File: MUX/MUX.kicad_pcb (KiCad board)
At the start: 4 copper layers, 364 x 203 mm, 135 parts, among them P1 Conn_02x36_Top_Bottom, P2 DB9_Male, P3 DB9_Male, P4 DB9_Male, P5 DB9_Male

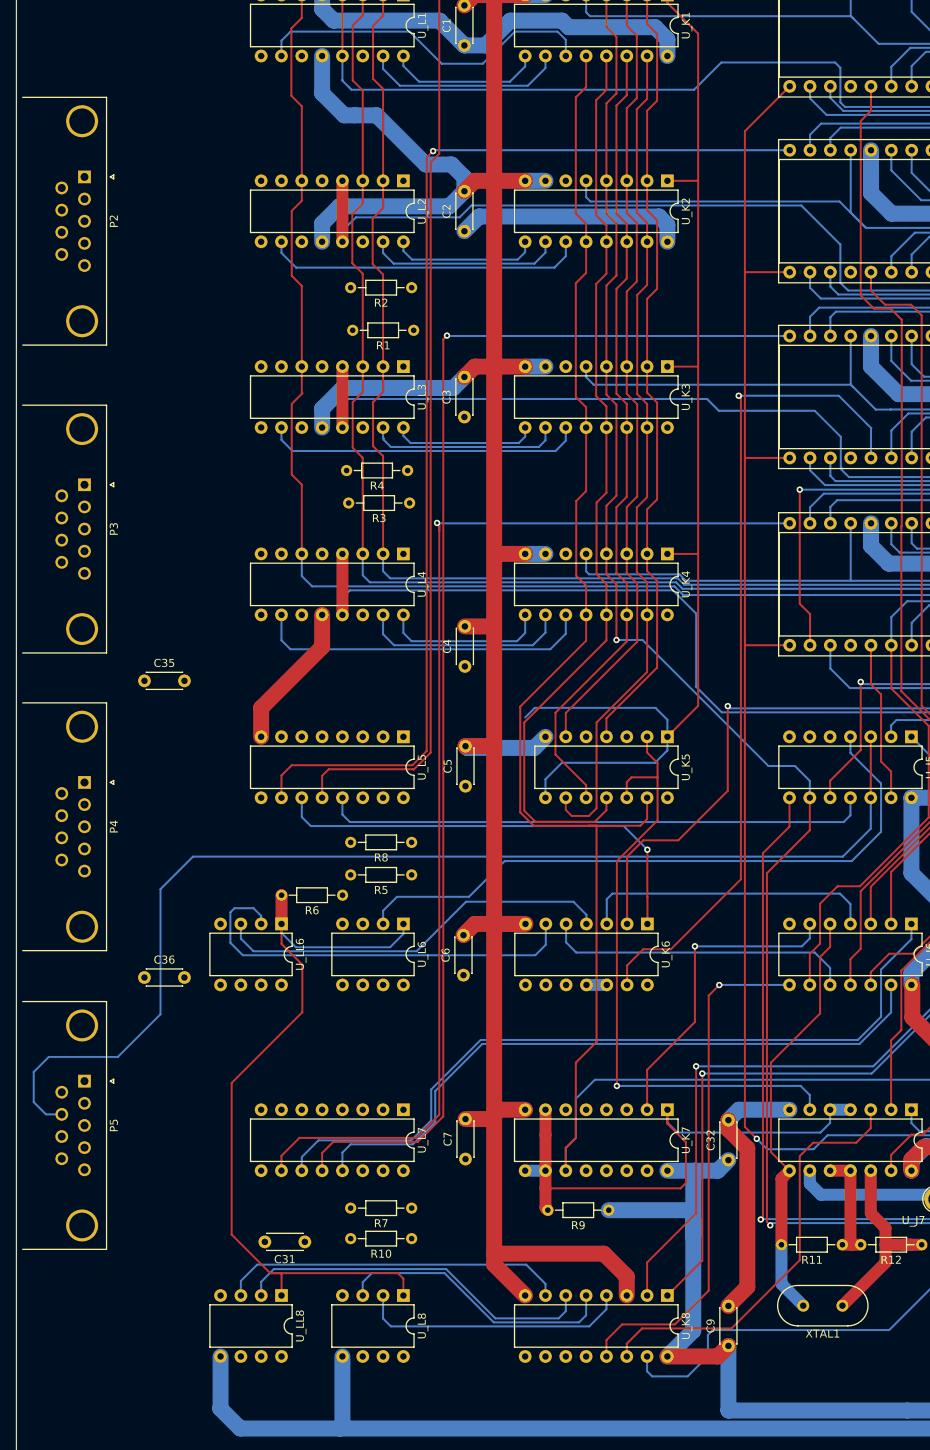
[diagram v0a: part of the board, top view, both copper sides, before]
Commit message: MUX: Add connector pinout switch jumpers
Provide jumper blocks to easily confiure MUX outputs as either Centuriobn native
or standard RS232 pinout. Provides for ease of use of USB adapters,
off-the-shelf cables, etc.
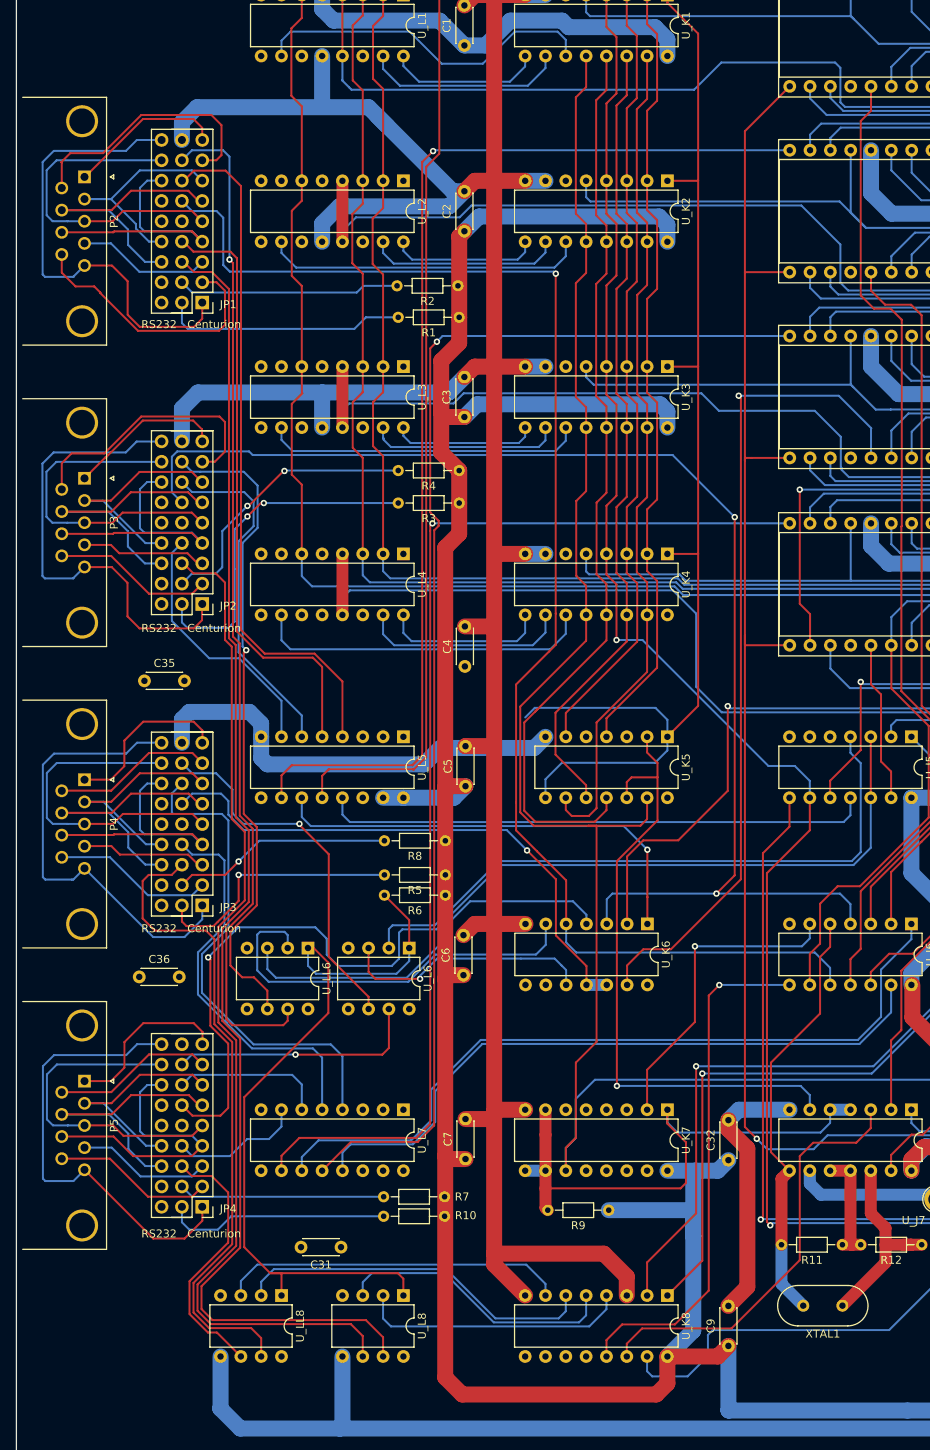
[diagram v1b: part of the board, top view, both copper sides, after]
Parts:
- added JP1: Jumper_3x9_Bridged12, Connector_PinHeader_2.54mm:PinHeader_3x09_P2.54mm_Vertical, F.Cu at (47.2, 79.1)
- added JP2: Jumper_3x9_Bridged12, Connector_PinHeader_2.54mm:PinHeader_3x09_P2.54mm_Vertical, F.Cu at (47.2, 116.8)
- added JP3: Jumper_3x9_Bridged12, Connector_PinHeader_2.54mm:PinHeader_3x09_P2.54mm_Vertical, F.Cu at (47.2, 154.4)
- added JP4: Jumper_3x9_Bridged12, Connector_PinHeader_2.54mm:PinHeader_3x09_P2.54mm_Vertical, F.Cu at (47.2, 192.1)
- moved R6 12.9 mm to (77.6, 153.2)
- moved R4 6.45 mm to (79.3, 100.1)
- moved R3 6.20 mm to (79.3, 104.1)
- moved R1 5.92 mm to (79.3, 80.9)
- moved R2 5.80 mm to (79.2, 77.0)
- moved R10 4.97 mm to (77.5, 193.3)
- moved C31 4.57 mm to (64.6, 197.2)
- moved U_LL6 4.48 mm to (60.5, 159.8)
- moved R7 4.35 mm to (77.5, 190.9)
- moved R8 4.22 mm to (77.6, 146.4)
- moved R5 4.22 mm to (77.6, 150.6)
- moved U_L6 3.10 mm to (73.1, 159.8)
- moved P3 0.80 mm to (32.5, 101.0)
- moved C36 0.65 mm to (39.4, 163.4)
- moved P4 0.34 mm to (32.5, 138.7)
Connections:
- P2 pad 1: GND -> Net-(JP1-Pad25)
- P2 pad 2: /~{CTS_{0}} -> Net-(JP1-Pad12)
- P2 pad 3: -12V -> Net-(JP1-Pad13)
- P2 pad 4: /~{RTS_{0}} -> Net-(JP1-Pad7)
- P2 pad 5: Net-(P2-Pad5) -> Net-(JP1-Pad1)
- P2 pad 6: /~{TX_{0}} -> Net-(JP1-Pad22)
- P2 pad 7: /~{TX_{0}_EIA} -> Net-(JP1-Pad16)
- P2 pad 8: /~{RX_{0}} -> Net-(JP1-Pad10)
- P2 pad 9: Net-(P2-Pad9) -> Net-(JP1-Pad4)
- P3 pad 1: GND -> Net-(P3-Pad1)
- P3 pad 2: /~{CTS_{1}} -> Net-(JP2-Pad12)
- P3 pad 3: -12V -> Net-(P3-Pad3)
- P3 pad 4: /~{RTS_{1}} -> Net-(P3-Pad4)
- P3 pad 6: /~{TX_{1}} -> Net-(P3-Pad6)
- P3 pad 7: /~{TX_{1}_EIA} -> Net-(JP2-Pad16)
- P3 pad 8: /~{RX_{1}} -> Net-(P3-Pad8)
- P4 pad 1: GND -> Net-(P4-Pad1)
- P4 pad 2: /~{CTS_{2}} -> Net-(JP3-Pad12)
- P4 pad 3: -12V -> Net-(P4-Pad3)
- P4 pad 4: /~{RTS_{2}} -> Net-(P4-Pad4)
- P4 pad 6: /~{TX_{2}} -> Net-(P4-Pad6)
- P4 pad 7: /~{TX_{2}_EIA} -> Net-(P4-Pad7)
- P4 pad 8: /~{RX_{2}} -> Net-(P4-Pad8)
- P5 pad 1: GND -> Net-(P5-Pad1)
- P5 pad 2: /~{CTS_{3}} -> Net-(P5-Pad2)
- P5 pad 3: -12V -> Net-(P5-Pad3)
- P5 pad 4: /~{RTS_{3}} -> Net-(P5-Pad4)
- P5 pad 6: /~{TX_{3}} -> Net-(P5-Pad6)
- P5 pad 7: /~{TX_{3}_EIA} -> Net-(P5-Pad7)
- P5 pad 8: /~{RX_{3}} -> Net-(P5-Pad8)
- R1 pad 2: Net-(P2-Pad5) -> Net-(JP1-Pad2)
- R10 pad 2: Net-(P5-Pad5) -> Net-(R10-Pad2)
- R2 pad 2: Net-(P2-Pad9) -> Net-(JP1-Pad5)
- R3 pad 2: Net-(P3-Pad5) -> Net-(R3-Pad2)
- R4 pad 2: Net-(P3-Pad9) -> Net-(JP2-Pad5)
- R5 pad 2: Net-(P4-Pad5) -> Net-(R5-Pad2)
- R7 pad 2: Net-(P5-Pad9) -> Net-(R7-Pad2)
- R8 pad 2: Net-(P4-Pad9) -> Net-(R8-Pad2)
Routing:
- net +5V: track 3327.7 -> 3557.8 mm
- net /~{RTS_{0}}: track 0.00 -> 167.4 mm
- net /~{TX_{0}_EIA}: track 38.8 -> 178.7 mm, vias 0 -> 1
- net /~{TX_{1}_EIA}: track 36.9 -> 165.1 mm, vias 0 -> 2
- net /~{RTS_{1}}: track 0.00 -> 127.2 mm
- net /~{TX_{0}}: track 0.00 -> 126.9 mm, vias 0 -> 1
- net /~{CTS_{0}}: track 0.00 -> 86.4 mm
- net /~{RTS_{2}}: track 0.00 -> 82.2 mm
- net /~{TX_{1}}: track 0.00 -> 82.0 mm, vias 0 -> 1
- net /~{RX_{0}}: track 0.00 -> 75.6 mm
- net GND: track 2840.1 -> 2914.3 mm
- net /~{TX_{2}_EIA}: track 2.54 -> 70.0 mm, vias 0 -> 1
- net /~{CTS_{2}}: track 0.00 -> 62.1 mm
- net Net-(P3-Pad5): track 0.00 -> 58.8 mm
- net Net-(JP1-Pad1): track 0.00 -> 58.8 mm
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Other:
- board text added: "RS232 Centurion"

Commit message: MUX: More power routing
All basic connections except 12V
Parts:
- moved C34 3.05 mm to (173.1, 119.7)
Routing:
- net GND: track 2914.3 -> 3322.5 mm, vias 4 -> 5
- net +5V: track 3557.8 -> 3790.0 mm
- net +12V: track 315.0 -> 355.2 mm
- net Net-(U_K1-Pad1): track 149.2 -> 128.2 mm
- net -12V: track 398.5 -> 415.7 mm
- net /LoadCR_{3}: track 200.1 -> 207.3 mm
- net /~{TX_{3}_EIA}: track 136.0 -> 143.1 mm
- net /Data.InBD_{2}: track 535.7 -> 542.8 mm
- net /~{RX_{3}}: track 16.6 -> 22.5 mm
- net /Data.OutD_{5}: track 417.0 -> 422.7 mm, vias 3 -> 4
- net Net-(U_E6-Pad1): track 29.9 -> 25.3 mm
- net Net-(U_J6-Pad8): track 64.9 -> 69.3 mm
- net Net-(U_H7-Pad15): track 227.8 -> 232.1 mm
- net /~{TX_{1}_EIA}: track 165.1 -> 169.4 mm
- net /Data.InBD_{6}: track 464.2 -> 467.8 mm
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
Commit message: MUX: Connections completed
All traces done
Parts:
- moved C8 15.4 mm to (112.5, 36.3)
- moved C35 4.39 mm to (44.4, 126.6)
- moved C36 3.61 mm to (43.0, 163.6)
- moved JP4 2.02 mm to (45.2, 192.1)
- moved JP1 2.02 mm to (45.2, 79.1)
- moved JP2 2.02 mm to (45.2, 116.8)
- moved JP3 2.02 mm to (45.2, 154.4)
- moved C31 0.18 mm to (64.8, 197.2)
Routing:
- net -12V: track 415.7 -> 756.0 mm, vias 2 -> 6
- net GND: track 3322.5 -> 3573.8 mm, vias 5 -> 7
- net +12V: track 355.2 -> 562.0 mm, vias 1 -> 2
- net +5V: track 3790.0 -> 3909.1 mm
- net /~{RX_{2}}: track 50.0 -> 59.4 mm
- net /~{CTS_{2}}: track 62.1 -> 71.5 mm
- net Net-(P5-Pad1): track 21.6 -> 14.6 mm
- net Net-(U_A1-Pad10): track 79.6 -> 73.0 mm
- net Net-(R6-Pad2): track 95.8 -> 102.3 mm
- net Sys.INT_OUT: track 117.4 -> 111.0 mm
- net Net-(P1-Pad30): track 0.00 -> 5.90 mm, vias 0 -> 1
- net Net-(JP1-Pad12): track 28.9 -> 24.4 mm
- net Net-(P5-Pad3): track 41.3 -> 37.2 mm
- net Net-(P4-Pad3): track 41.3 -> 37.2 mm
- net Net-(JP1-Pad13): track 41.3 -> 37.3 mm
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
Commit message: MUX: Proper crystal
Use HC-49U crystal. Elements rearranged to match the original layout, just for
fun. Some more power optimizations.
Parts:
- XTAL1: footprint Crystal:Crystal_HC18-U_Vertical -> Crystal:Crystal_HC49-U_Horizontal
- moved R20 19.6 mm to (146.8, 199.5)
- moved R21 8.71 mm to (141.7, 180.6), turned to -90 degrees
- moved XTAL1 6.25 mm to (124.5, 198.9), turned to 0 degrees
- moved TP1 4.99 mm to (142.5, 194.7)
- moved R11 2.18 mm to (127.3, 194.7)
- moved R12 2.18 mm to (137.2, 194.7)
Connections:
- JP4 pad 15: (no net) -> unconnected-(JP4-Pad15)
- JP4 pad 18: (no net) -> unconnected-(JP4-Pad18)
- JP4 pad 3: (no net) -> unconnected-(JP4-Pad3)
- JP4 pad 6: (no net) -> unconnected-(JP4-Pad6)
- XTAL1 pad 1: Net-(R12-Pad1) -> Net-(R11-Pad2)
- XTAL1 pad 2: Net-(R11-Pad2) -> Net-(R12-Pad1)
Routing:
- net GND: track 3573.8 -> 3761.5 mm
- net +5V: track 3909.1 -> 3839.5 mm
- net /MUXClock: track 441.5 -> 451.2 mm
- net Net-(R21-Pad2): track 20.7 -> 28.5 mm
- net Net-(R12-Pad1): track 24.4 -> 19.1 mm
- net Net-(U_J7-Pad6): track 78.8 -> 84.0 mm
- net Net-(R20-Pad2): track 10.9 -> 16.0 mm
- net Net-(U_H7-Pad15): track 230.7 -> 227.1 mm
- net Net-(U_H7-Pad9): track 120.0 -> 117.0 mm
- net Net-(R11-Pad2): track 51.4 -> 48.6 mm
- net Net-(R11-Pad1): track 14.1 -> 11.9 mm
- net /RxD_{2}: track 106.1 -> 104.4 mm
- net /RX_{3}_IN: track 141.9 -> 143.3 mm
- net /RX_{1}_IN: track 142.0 -> 143.3 mm
- net /Data.InBD_{1}: track 544.2 -> 545.5 mm
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
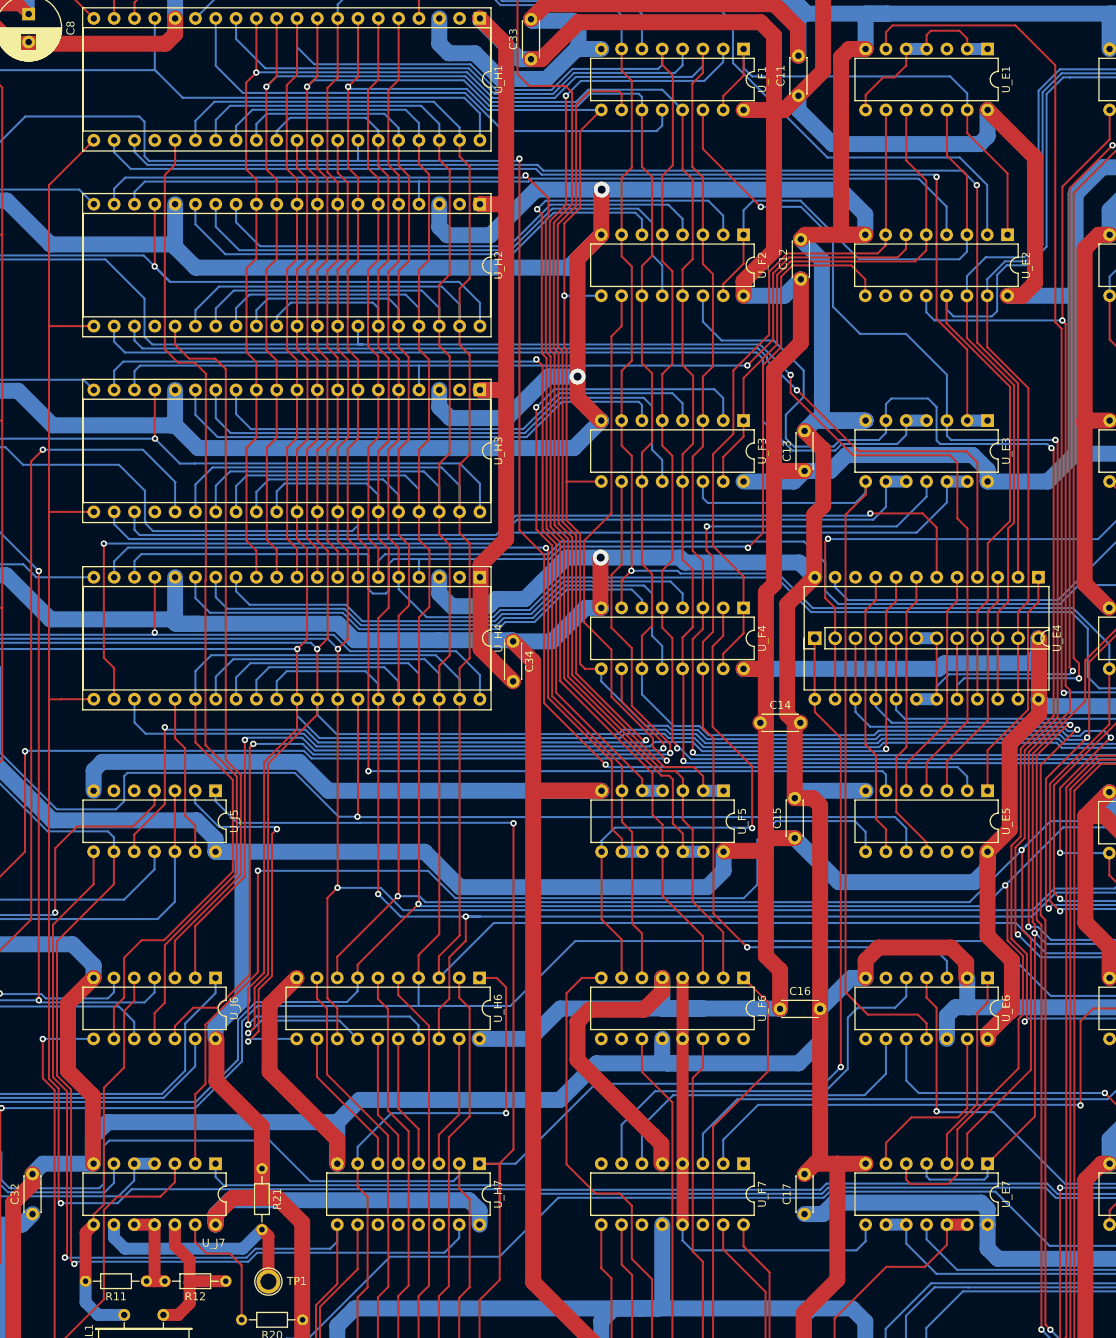
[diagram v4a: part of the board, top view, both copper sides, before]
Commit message: MUX: Fix DRC errors
Rearranged U_E4 socket and extra row in order to avoid overlap errors. Fixed up
jumper block courtyards.
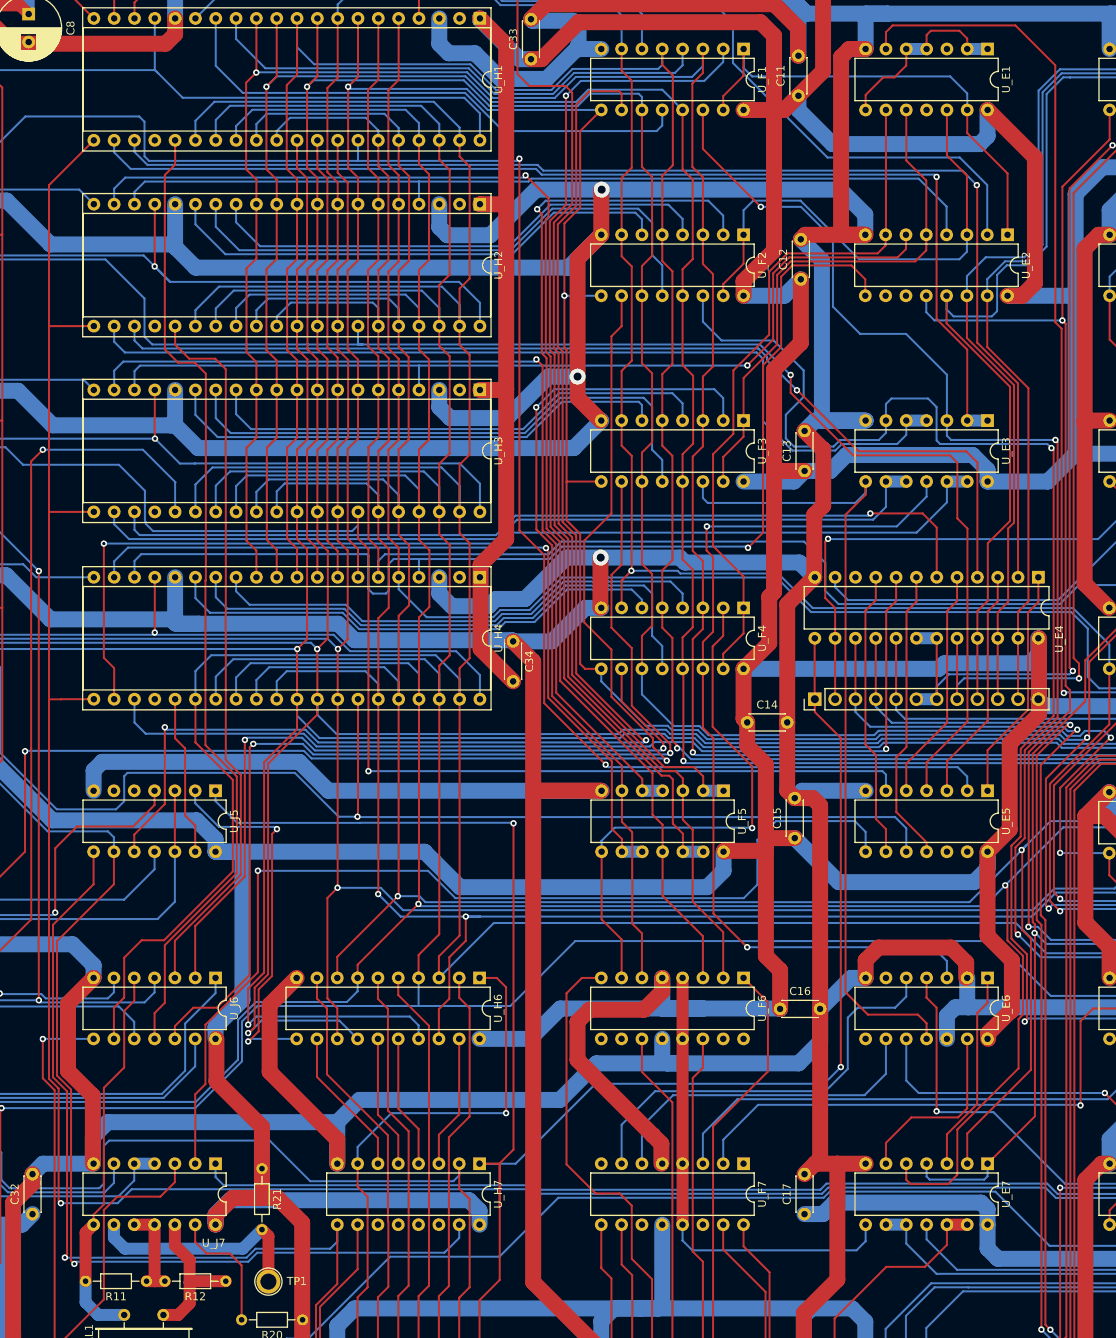
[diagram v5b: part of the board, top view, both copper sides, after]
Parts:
- U_E4: footprint Package_DIP:DIP-24_W15.24mm -> Package_DIP:DIP-24_W7.62mm
- moved U_EB4 7.62 mm to (210.8, 121.9)
- moved C14 1.64 mm to (202.3, 124.8)
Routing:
- net GND: track 3761.5 -> 3760.8 mm
- net +5V: track 3839.5 -> 3838.8 mm

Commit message: MUX: Move connectors
Move connectors to the center in order to provide the necessary space for
pullers.
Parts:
- moved C36 17.6 mm to (57.0, 152.9), turned to 180 degrees
- moved P2 6.28 mm to (32.5, 69.7)
- moved JP1 6.28 mm to (45.2, 85.4)
- moved JP4 6.09 mm to (45.2, 186.0)
- moved P5 6.09 mm to (32.5, 170.3)
- moved JP2 2.16 mm to (45.3, 118.9)
- moved P3 2.15 mm to (32.5, 103.2)
- moved P4 1.97 mm to (32.5, 136.8)
- moved JP3 1.96 mm to (45.2, 152.5)
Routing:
- net /~{TX_{3}_EIA}: track 142.3 -> 124.3 mm
- net /~{TX_{0}}: track 122.6 -> 135.0 mm
- net GND: track 3760.8 -> 3772.2 mm, vias 7 -> 8
- net -12V: track 756.0 -> 745.9 mm
- net /~{CTS_{2}}: track 71.5 -> 63.7 mm
- net /~{RX_{2}}: track 59.4 -> 51.8 mm
- net /~{RX_{0}}: track 77.6 -> 71.0 mm
- net /~{TX_{0}_EIA}: track 182.3 -> 175.7 mm
- net /~{RTS_{3}}: track 32.4 -> 38.5 mm
- net /~{CTS_{0}}: track 88.5 -> 82.7 mm
- net Net-(JP4-Pad5): track 27.8 -> 33.4 mm
- net Net-(R6-Pad2): track 102.3 -> 107.9 mm
- net /~{RX_{3}}: track 23.3 -> 18.1 mm
- net /~{RTS_{0}}: track 166.8 -> 163.5 mm
- net Net-(JP1-Pad5): track 29.8 -> 32.4 mm
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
